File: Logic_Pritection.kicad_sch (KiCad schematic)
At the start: 10 parts

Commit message: VER2.2: все изменения в списке изменений
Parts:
- D2, D3: value ADM3485E -> ~; Description P/N (none) -> RS485; Product Name (none) -> SN65HVD3082EDR

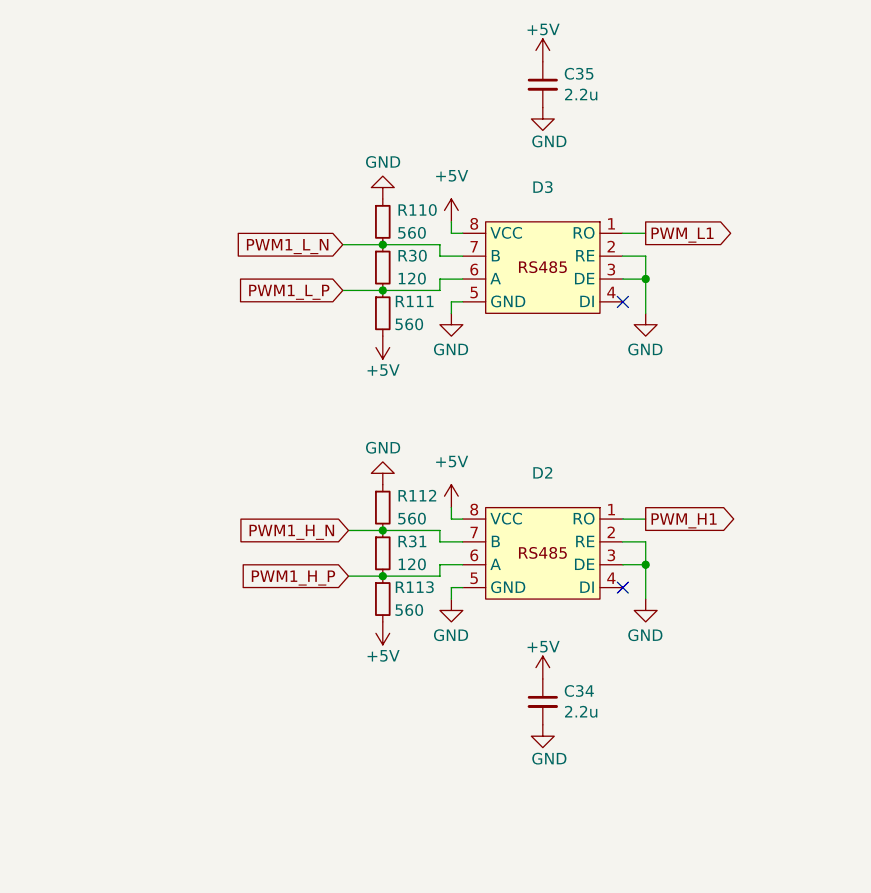
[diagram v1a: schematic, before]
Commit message: VER2.2: добавил фильтры на вход ШИМа и обновил все доки
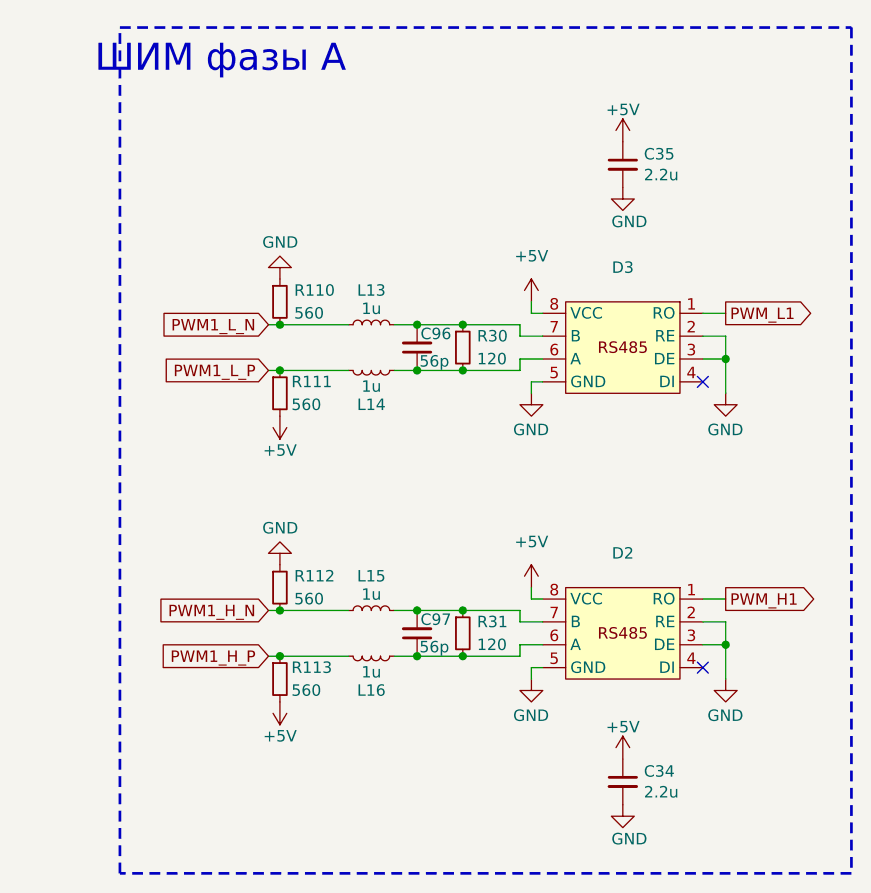
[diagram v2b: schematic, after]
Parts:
- added C96, C97: 56p, Capacitor_SMD:C_0805_2012Metric_Pad1.18x1.45mm_HandSolder, symbol Device:C_Small
- added L13, L14, L15, L16: 1u, Inductor_SMD:L_0603_1608Metric_Pad1.05x0.95mm_HandSolder, symbol Device:L_Small
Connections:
- net PWM1_H_N: now also L15.1; no longer D2.7 (B), R31.1
- net PWM1_H_P: now also L16.2; no longer D2.6 (A), R31.2
- net PWM1_L_N: now also L13.1; no longer D3.7 (B), R30.1
- net PWM1_L_P: now also L14.2; no longer D3.6 (A), R30.2
- new net: C97.1, D2.6 (A), L16.1, R31.2
- new net: C96.1, D3.6 (A), L14.1, R30.2
- new net: C96.2, D3.7 (B), L13.2, R30.1
- new net: C97.2, D2.7 (B), L15.2, R31.1
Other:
- note added: "ШИМ фазы А"
- company: (none) -> ООО "ЭТТ"
- moved on the sheet: C34, C35, D2, D3, R110, R111, R112, R113, R30, R31
